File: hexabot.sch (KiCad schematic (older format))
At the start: 1 part

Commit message: Start schematic
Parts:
- added C? (x2): 20p, symbol C
- added D?: LEDR, symbol LED
- added D?: LEDY, symbol LED
- added D?: LEDG, symbol LED
- added JP?: JUMPER, symbol JUMPER
- added LOGO?: OPEN_HARDWARE_1, symbol OPEN_HARDWARE_1
- added P?: PICKIT, symbol CONN_01X05
- added P?: USB_B, symbol USB_B
- added P?: CONN_01X04, symbol CONN_01X04
- added R? (x3): 330R, symbol R
- added R?: 1M, symbol R
- added Y?: Crystal, symbol Crystal
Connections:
- net at U?.10 (VDD): now also U?.19 (AVDD), U?.26 (VDD), U?.38 (VDD)
- net GND: now reaches U?.20 (AVSS)
- net GND: now also U?.25 (VSS), U?.41 (VSS), U?.9 (VSS), C?.1, C?.1, D?.1 (K), D?.1 (K), D?.1 (K), P?.1 (P1), P?.4 (GND)
- net OSC1: now reaches U?.39 (OSC1/RPI60/RC12)
- net OSC1: now also C?.2, R?.1, Y?.1
- net OSC2: now reaches U?.40 (OSC2/CLKO/RC15)
- net OSC2: now also C?.2, R?.2, Y?.2
- net LEDR: now reaches U?.46 (INT0/DMH/RP64/RD0)
- net LEDR: now also P?.2 (P2), R?.1
- net PGED: now reaches U?.47 (PGED2/SOSCI/C3IN3-/RPI61/RC13)
- net PGED: now also P?.3 (P3)
- net PGEC: now reaches U?.48 (PGEC2/SOSCO/C3IN1-/T1CK/RPI62/RC14)
- net PGEC: now also P?.4 (P4)
- net LEDY: now reaches U?.49 (VCPCON/RP65/RD1)
- net LEDY: now also P?.3 (P3), R?.1
- net LEDG: now reaches U?.50 (DPH/RP66/RD2)
- net LEDG: now also P?.4 (P4), R?.1
- net +3V3: now reaches U?.57 (VDD)
- net +3V3: now also P?.2 (P2)
- net MCLR: now reaches U?.7 (~MCLR)
- net MCLR: now also P?.1 (P1)
- new net: D?.2 (A), R?.2 (x3)
- new net: JP?.2, P?.1 (VCC)
- new net +5V: JP?.1
- new net D+: P?.3 (D+)
- new net D-: P?.2 (D-)
- no-connect marks 0 -> 1
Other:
- moved on the sheet: U?

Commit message: More sch
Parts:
- removed P?: CONN_01X04, symbol CONN_01X04
- added C? (x7): 100n, symbol C
- added C?: 10u, symbol CP
- added C? (x2): 2u2, symbol C
- added C? (x2): 330u, symbol CP
- added C? (x2): 4u7, symbol C
- added C? (x2): 15n, symbol C
- added JP?: JUMPER, symbol JUMPER
- added MH? (x4): HOLE_M3, symbol HOLE_M3
- added P?: NC, symbol CONN_01X05
- added P?: SERVO1, symbol CONN_01X03
- added P?: NC, symbol CONN_01X06
- added P?: NC, symbol CONN_01X04
- added P?: ENC4, symbol CONN_01X04
- added P?: ENC3, symbol CONN_01X04
- added P?: ENC2, symbol CONN_01X04
- added P?: ENC1, symbol CONN_01X04
- added P?: UART_1_5V, symbol CONN_01X04
- added P?: UART_2_3V3, symbol CONN_01X06
- added P?: DEBUG, symbol CONN_01X05
- added P?: BATTERY, symbol CONN_01X02
- added P?: SERVO2, symbol CONN_01X03
- added P?: DYNAMIXEL, symbol CONN_01X03
- added Q? (x4): Q_NMOS_GSD, symbol Q_NMOS_GSD
- added R?: 330R, symbol R
- added R?: 4K7, symbol R
- added R?: 0, symbol R
- added R?: 0R, symbol R
- added R?: 1k, symbol R
- added R?: 21k, symbol R
- added R?: 7k52, symbol R
- added R? (x2): 10k, symbol R
- added SW?: PUSH1, symbol SPST
- added SW?: PUSH2, symbol SPST
- added U?: PTN78020 +5V, symbol PTN78020
- added U?: L6201PS, symbol L6201PS
- added U?: MCP1727, symbol MCP1727
- added U?: PTN78020 SERVO, symbol PTN78020
- C? (x2): value 20p -> 18p
- R? (x3): value 330R -> 470R
- Y?: value Crystal -> 8M
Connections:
- net labels added: +BATT, AN3, AVSS, DYNAMIXEL, ENC_1_A, ENC_1_B, ENC_2_A, ENC_2_B, ENC_3_A, ENC_3_B, ENC_4_A, ENC_4_B, MOTOR_L_DIR1, MOTOR_L_DIR2, MOTOR_L_PWM, MOTOR_R_DIR1, MOTOR_R_DIR2, MOTOR_R_OUT1, MOTOR_R_OUT2, MOTOR_R_PWM, PUSH_1, PUSH_2, PWR_SERVO, REG_SERVO, RX1, RX2, SCK, SCL, SDA, SDI, SDO, SENSE_L, SENSE_R, SERVO_1, SERVO_2, TX1, TX2, USB_SHIELD, VREF, ~CTS2, ~RTS2
- wire segments 33 -> 198
- no-connect marks 1 -> 4
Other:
- note added: "1% 50mW"
- note added: "1% 50mW\nVO=7.4V\nfor XL-320"
- note added: "5V Tolerant"
- note added: "TODO: sheet"
- moved on the sheet: C?, D?, JP?, LOGO?, P?, R?, U?, Y?

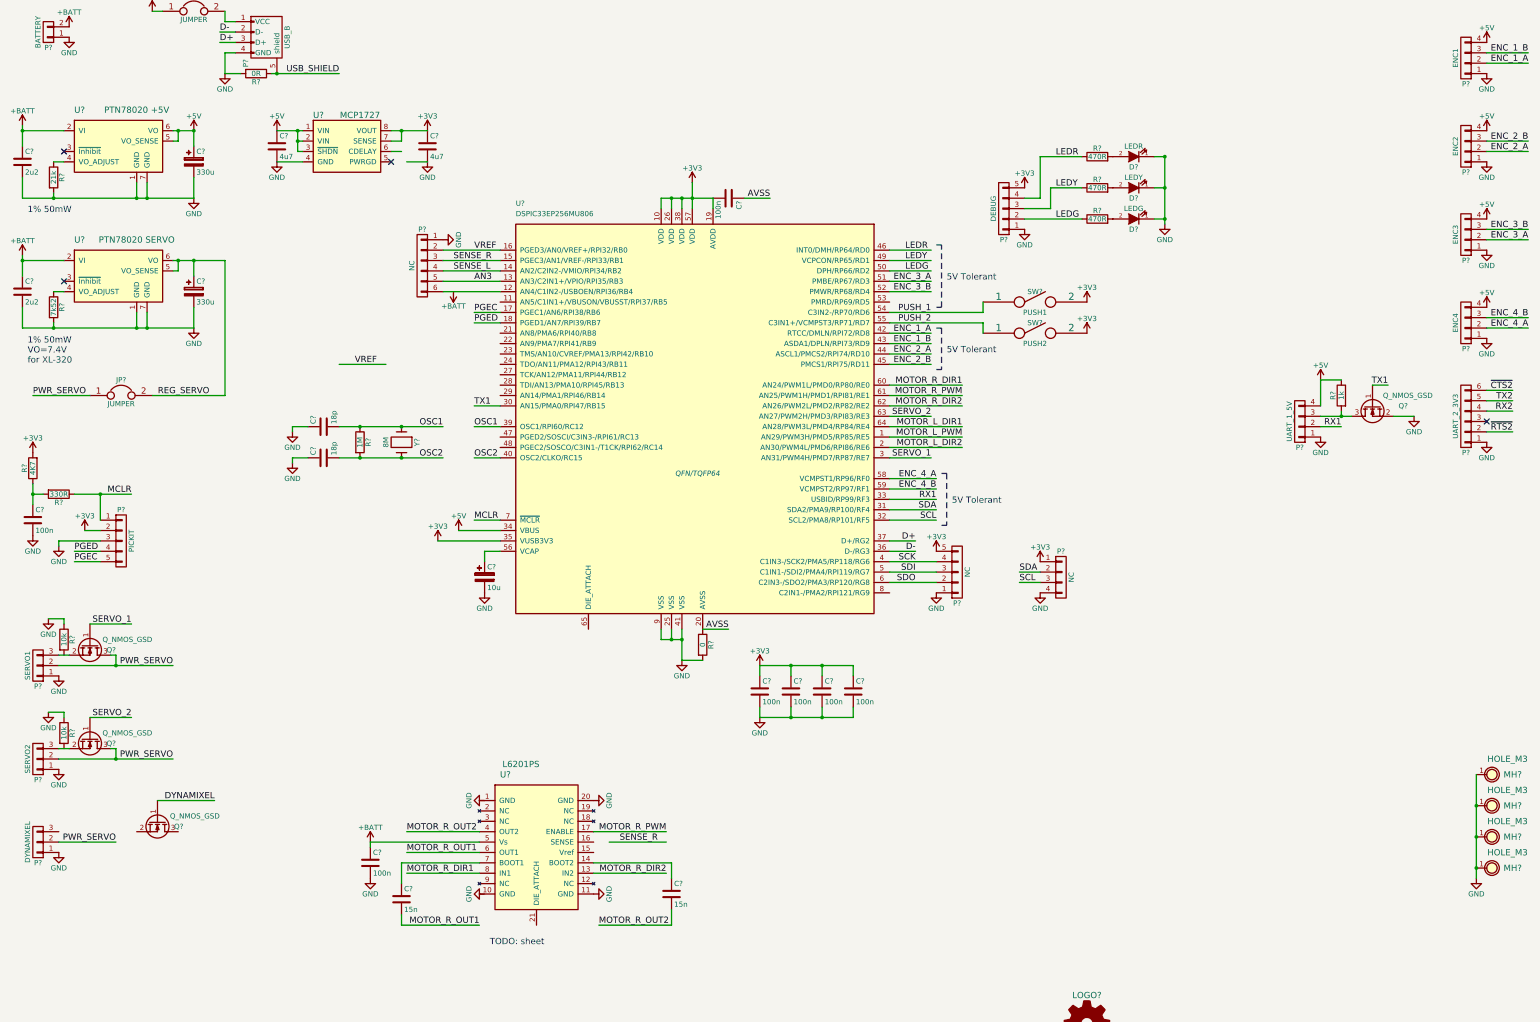
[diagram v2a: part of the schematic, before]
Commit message: Subsheet for drivers
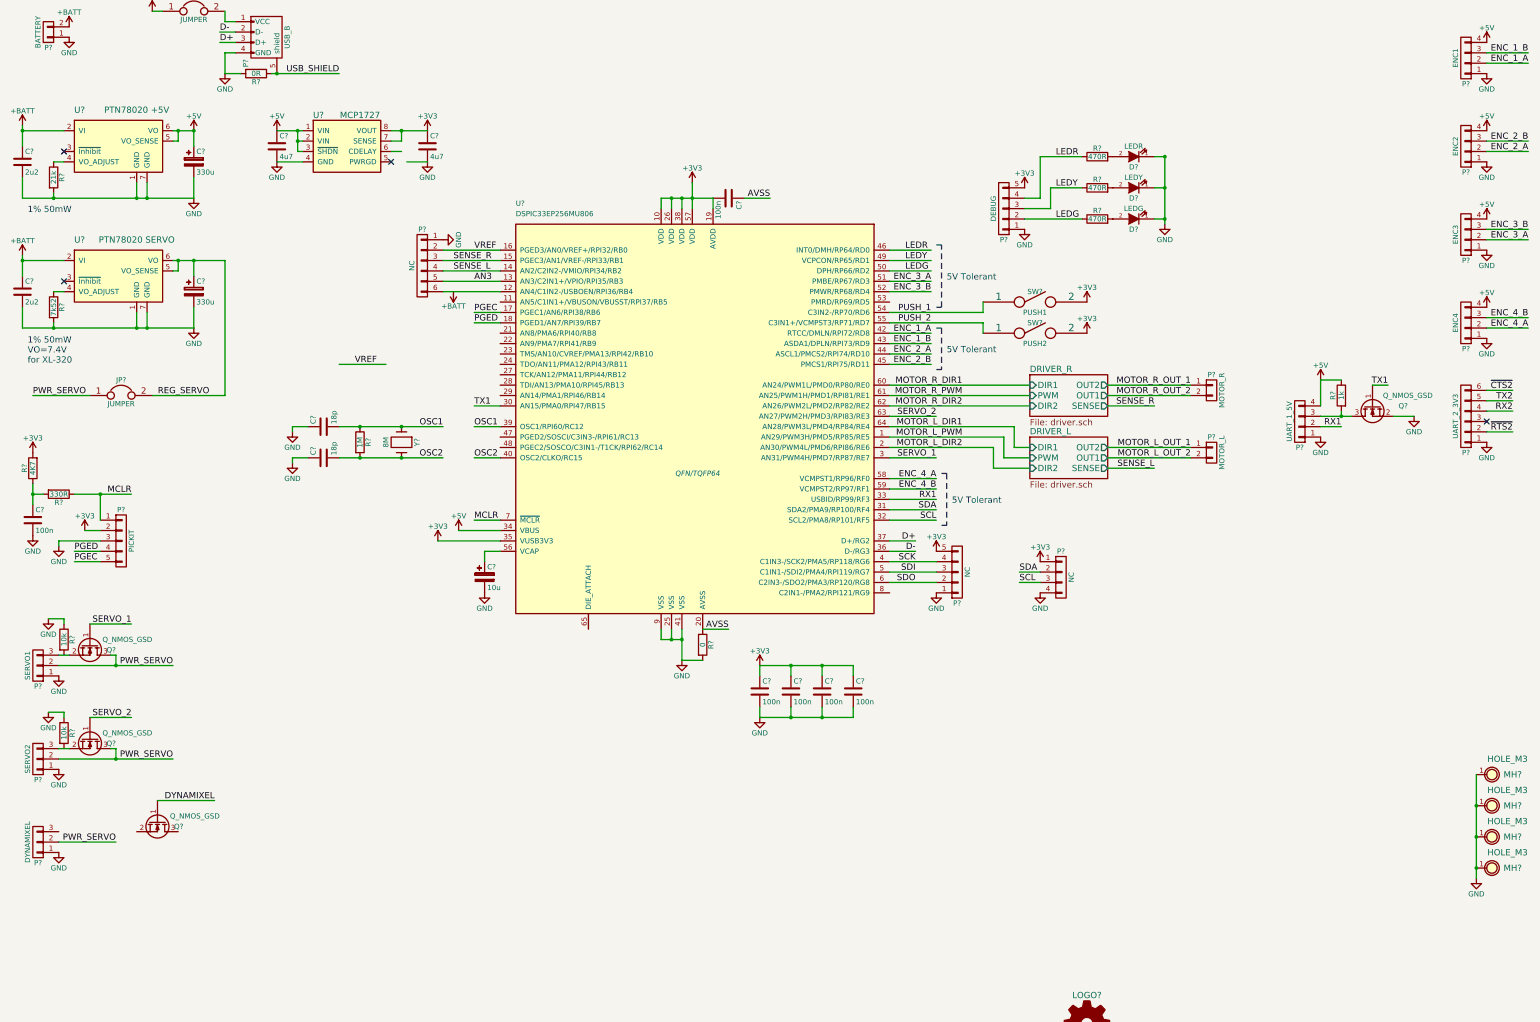
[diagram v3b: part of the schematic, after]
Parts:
- removed C?: 100n, symbol C
- removed C? (x2): 15n, symbol C
- removed U?: L6201PS, symbol L6201PS
- added P?: MOTOR_R, symbol CONN_01X02
- added P?: MOTOR_L, symbol CONN_01X02
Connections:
- net labels added: MOTOR_L_OUT_1, MOTOR_L_OUT_2, MOTOR_R_OUT_1, MOTOR_R_OUT_2
- net labels removed: MOTOR_R_OUT1, MOTOR_R_OUT2
- wire segments 198 -> 233
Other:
- note removed: "TODO: sheet"

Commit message: Most of sch ready
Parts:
- removed P?: NC, symbol CONN_01X04
- added C26: NC, symbol C
- added D1: D, symbol D
- added D10, D7, D8, D9: LEDB, symbol LED
- added D2: TL431DBZ, SOT-23, symbol TL431DBZ
- added D3: ZENER, symbol ZENER
- added F1: FUSE, symbol FUSE
- added JP2: JUMPER, symbol JUMPER
- added P10: BUMP2, symbol CONN_01X02
- added P2: EXT_POWER, symbol CONN_01X02
- added P22: NC, symbol CONN_01X06
- added P23: START, symbol CONN_01X02
- added P7: PANIC BUTTON, symbol CONN_01X02
- added P9: BUMP1, symbol CONN_01X02
- added R10, R11, R9: 100R, symbol R
- added R12, R16, R35: 1k, symbol R
- added R13, R14, R15: 0R, symbol R
- added R22, R23, R24, R25: 470R, symbol R
- added R26, R27, R7: 10k, symbol R
- P16: renamed from P?; value UART_1_5V -> UART1_5V
- P21: renamed from P?; value UART_2_3V3 -> UART2_3V3
- R18: renamed from R?; value 0 -> 0R
- gave numbers to parts that had none: 63
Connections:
- net +3V3: now also Q3.1 (G), D2.1 (K), P22.4 (P4), R25.1
- net +5V: now also P22.6 (P6), R24.1
- net +BATT: now also P8.6 (P6), F1.2, P7.1 (P1), R16.2, R22.1; no longer C2.1, P1.2 (P2), U2.2 (VI)
- net AN3: now also R11.1, R15.1; no longer P8.5 (P5)
- net DYNAMIXEL: now also Q3.2 (S), U4.29 (AN14/PMA1/RPI46/RB14); no longer Q3.1 (G)
- net GND: now also C26.2, D10.1 (K), D2.3 (A), D3.2 (A), D7.1 (K), D8.1 (K), D9.1 (K), P10.1 (P1), P2.1 (P1), P22.1 (P1), P23.1 (P1), P9.1 (P1), R10.2, R11.2, R12.2, R9.2
- net PWR_SERVO: no longer P5.2 (P2)
- net REG_SERVO: now also JP2.2, R23.1
- net RX2: now also U4.23 (TMS/AN10/CVREF/PMA13/RPI42/RB10)
- net SCL: now also P22.2 (P2), R27.1
- net SDA: now also P22.3 (P3), R26.2
- net SENSE_L: now also R14.2; no longer U4.14 (AN2/C2IN2-/VMIO/RPI34/RB2)
- net SENSE_R: now also R13.1; no longer U4.15 (PGEC3/AN1/VREF-/RPI33/RB1)
- net TX2: now also U4.22 (AN9/PMA7/RPI41/RB9)
- net VREF: now also D2.2 (REF)
- net ~CTS2: now also U4.21 (AN8/PMA6/RPI40/RB8)
- net ~RTS2: now also U4.24 (TDO/AN11/PMA12/RPI43/RB11)
- net AN4: now reaches U4.12 (AN4/C1IN2-/USBOEN/RPI36/RB4)
- net AN4: now also R12.1, R16.1; no longer P8.6 (P6)
- net ~PANIC: now reaches U4.27 (TCK/AN12/PMA11/RPI44/RB12)
- net ~PANIC: now also D3.1 (K), R35.1
- net START: now reaches U4.28 (TDI/AN13/PMA10/RPI45/RB13)
- net START: now also P23.2 (P2)
- net BUMP_1: now reaches U4.47 (PGED2/SOSCI/C3IN3-/RPI61/RC13)
- net BUMP_1: now also P9.2 (P2)
- net BUMP_2: now reaches U4.48 (PGEC2/SOSCO/C3IN1-/T1CK/RPI62/RC14)
- net BUMP_2: now also P10.2 (P2)
- net at P3.3 (P3), Q1.2 (S): now also R5.2
- net CDELAY: now reaches U3.6 (CDELAY)
- net CDELAY: now also C26.1
- net at P4.3 (P3), Q2.2 (S): now also R6.2
- net DYN_DATA: now reaches P5.3 (P3)
- net DYN_DATA: now also Q3.3 (D), R7.1
- new net: D7.2 (A), R22.2
- new net: D8.2 (A), R23.2
- new net: D10.2 (A), R25.2
- new net: D9.2 (A), R24.2
- new net: D1.2 (A), P1.2 (P2)
- new net: D1.1 (K), F1.1, P2.2 (P2)
- new net AN1: R13.2, R9.1, U4.15 (PGEC3/AN1/VREF-/RPI33/RB1)
- new net AN2: R10.1, R14.1, U4.14 (AN2/C2IN2-/VMIO/RPI34/RB2)
- new net AN3_FULL: P8.5 (P5), R15.2
- new net DYN_POWER: JP2.1, P5.2 (P2), R7.2
- new net I2C_POWER: P22.5 (P5), R26.1, R27.2
- new net MOTOR_POWER: C2.1, P7.2 (P2), R35.2, U2.2 (VI)
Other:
- note added: "Bidir Level Shifter"
- note added: "JUMPER"
- note added: "TODO: check NO / NC"
- note added: "TODO: check if zener needed"
- note added: "TODO: check impedances"
- note added: "TODO: connect\n"
- note added: "TODO: resistor values / zeners"
- note added: "soft pull down"
- note added: "soft pull up"
- moved on the sheet: C1, C10, C11, C12, C13, C14, C15, C2, C3, C4, C5, C6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

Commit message: Probably ready for layout
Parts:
- removed D2: TL431DBZ, SOT-23, symbol TL431DBZ
- added D?: ZENER, symbol ZENER
- added P?: DYNAMIXEL2, symbol CONN_01X03
- P5: value DYNAMIXEL -> DYNAMIXEL1
- R10, R11, R9: value 100R -> NC
- R12: value 1k -> 9k
- R13, R14, R15: value 0R -> NC
- R22: value 470R -> 10k
- R23: value 470R -> 2k
- R24: value 470R -> 1k
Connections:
- net AN4: now also D?.1 (K)
- net DYN_DATA: now also P?.3 (P3)
- net DYN_POWER: now also P?.2 (P2)
- net GND: now also U4.65 (DIE_ATTACH), D?.2 (A), P?.1 (P1)
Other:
- note removed: "TODO: check NO / NC"
- note removed: "TODO: check if zener needed"
- note removed: "TODO: check impedances"
- note removed: "TODO: connect\n"
- note removed: "TODO: resistor values / zeners"
- moved on the sheet: P8, R10, R11, R12, R13, R14, R15, R16, R9

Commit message: DRC
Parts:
- added P25, P26, P27: NC, symbol CONN_01X01
- gave numbers to parts that had none: 2
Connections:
- net GPIO_1: now reaches U4.11 (AN5/C1IN1+/VBUSON/VBUSST/RPI37/RB5)
- net GPIO_1: now also P25.1 (P1)
- net GPIO_3: now reaches U4.53 (PMRD/RP69/RD5)
- net GPIO_3: now also P27.1 (P1)
- net GPIO_2: now reaches U4.8 (C2IN1-/PMA2/RPI121/RG9)
- net GPIO_2: now also P26.1 (P1)

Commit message: Partial footprint association
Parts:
- C1, C10, C11, C12, C13, C14, C15, C2, C26, C3, C6, C7, C8, C9, R1, R10, R11, R12, R13, R14, R15, R16, R17, R18, R19, R2, R20, R21, R22, R23, R24, R25, R26, R27, R28, R3, R35, R4, R5, R6, R7, R8, R9: footprint (none) -> hexabot:R_0805_HandSoldering
- C4: footprint (none) -> hexabot:c_elec_8x10.5
- C5: footprint (none) -> hexabot:c_elec_10x10.5
- JP1, JP2, JP3: footprint (none) -> Pin_Headers:Pin_Header_Straight_1x02
- P10, P14, P15, P23, P9: footprint (none) -> Sockets_MOLEX_KK-System:Socket_MOLEX-KK-RM2-54mm_Lock_2pin_straight
- P11: footprint (none) -> hexabot:MICRO-B_USB
- P12, P6: footprint (none) -> Pin_Headers:Pin_Header_Straight_1x05
- P13: footprint (none) -> Sockets_MOLEX_KK-System:Socket_MOLEX-KK-RM2-54mm_Lock_5pin_straight
- P16, P17, P18, P19, P20: footprint (none) -> Sockets_MOLEX_KK-System:Socket_MOLEX-KK-RM2-54mm_Lock_4pin_straight
- P21, P8: footprint (none) -> Pin_Headers:Pin_Header_Straight_1x06
- P22: footprint (none) -> Sockets_MOLEX_KK-System:Socket_MOLEX-KK-RM2-54mm_Lock_6pin_straight
- P25, P26, P27: footprint (none) -> Pin_Headers:Pin_Header_Straight_1x01
- P3, P4: footprint (none) -> Pin_Headers:Pin_Header_Straight_1x03
- Q1, Q2, Q3, Q4: footprint (none) -> Housings_SOT-23_SOT-143_TSOT-6:SOT-23_Handsoldering
- U1, U2: footprint (none) -> hexabot:PTN78020H
- U3: footprint (none) -> hexabot:SOIC-8_3.9x4.9mm_Pitch1.27mm
- U4: footprint QFN/TQFP64 -> hexabot:QFN-64-1EP_9x9mm_Pitch0.5mm
- Y1: footprint (none) -> hexabot:Crystal_HC49-SD_SMD

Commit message: Remove KK for motors
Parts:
- P12: footprint Pin_Headers:Pin_Header_Straight_1x05 -> Sockets_MOLEX_KK-System:Socket_MOLEX-KK-RM2-54mm_Lock_5pin_straight
- P14, P15: footprint Sockets_MOLEX_KK-System:Socket_MOLEX-KK-RM2-54mm_Lock_2pin_straight -> (none)
- P21: value UART2_3V3 -> UART2_FTDI3V3
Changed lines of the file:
@@
 P 14800 4750
 F 0 "P21" H 14800 5100 50  0000 C CNN
-F 1 "UART2_3V3" V 14900 4750 50  0000 C CNN
+F 1 "UART2_FTDI3V3" V 14900 4750 50  0000 C CNN
 F 2 "Pin_Headers:Pin_Header_Straight_1x06" H 14800 4750 60  0001 C CNN
 F 3 "" H 14800 4750 60  0000 C CNN
@@
 F 0 "P12" H 9800 1950 50  0000 C CNN
 F 1 "DEBUG" V 9900 1650 50  0000 C CNN
-F 2 "Pin_Headers:Pin_Header_Straight_1x05" H 9800 1650 60  0001 C CNN
+F 2 "Sockets_MOLEX_KK-System:Socket_MOLEX-KK-RM2-54mm_Lock_5pin_straight" H 9800 1650 60  0001 C CNN
 F 3 "" H 9800 1650 60  0000 C CNN
 	1    9800 1650
@@
 F 0 "P14" H 13000 5650 50  0000 C CNN
 F 1 "MOTOR_R" V 13100 5500 50  0000 C CNN
-F 2 "Sockets_MOLEX_KK-System:Socket_MOLEX-KK-RM2-54mm_Lock_2pin_straight" H 13000 5500 60  0001 C CNN
+F 2 "" H 13000 5500 60  0000 C CNN
 F 3 "" H 13000 5500 60  0000 C CNN
 	1    13000 5500
@@
 F 0 "P15" H 13000 6450 50  0000 C CNN
 F 1 "MOTOR_L" V 13100 6300 50  0000 C CNN
-F 2 "Sockets_MOLEX_KK-System:Socket_MOLEX-KK-RM2-54mm_Lock_2pin_straight" H 13000 6300 60  0001 C CNN
+F 2 "" H 13000 6300 60  0001 C CNN
 F 3 "" H 13000 6300 60  0000 C CNN
 	1    13000 6300
